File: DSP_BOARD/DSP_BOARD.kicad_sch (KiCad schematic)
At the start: 0 parts

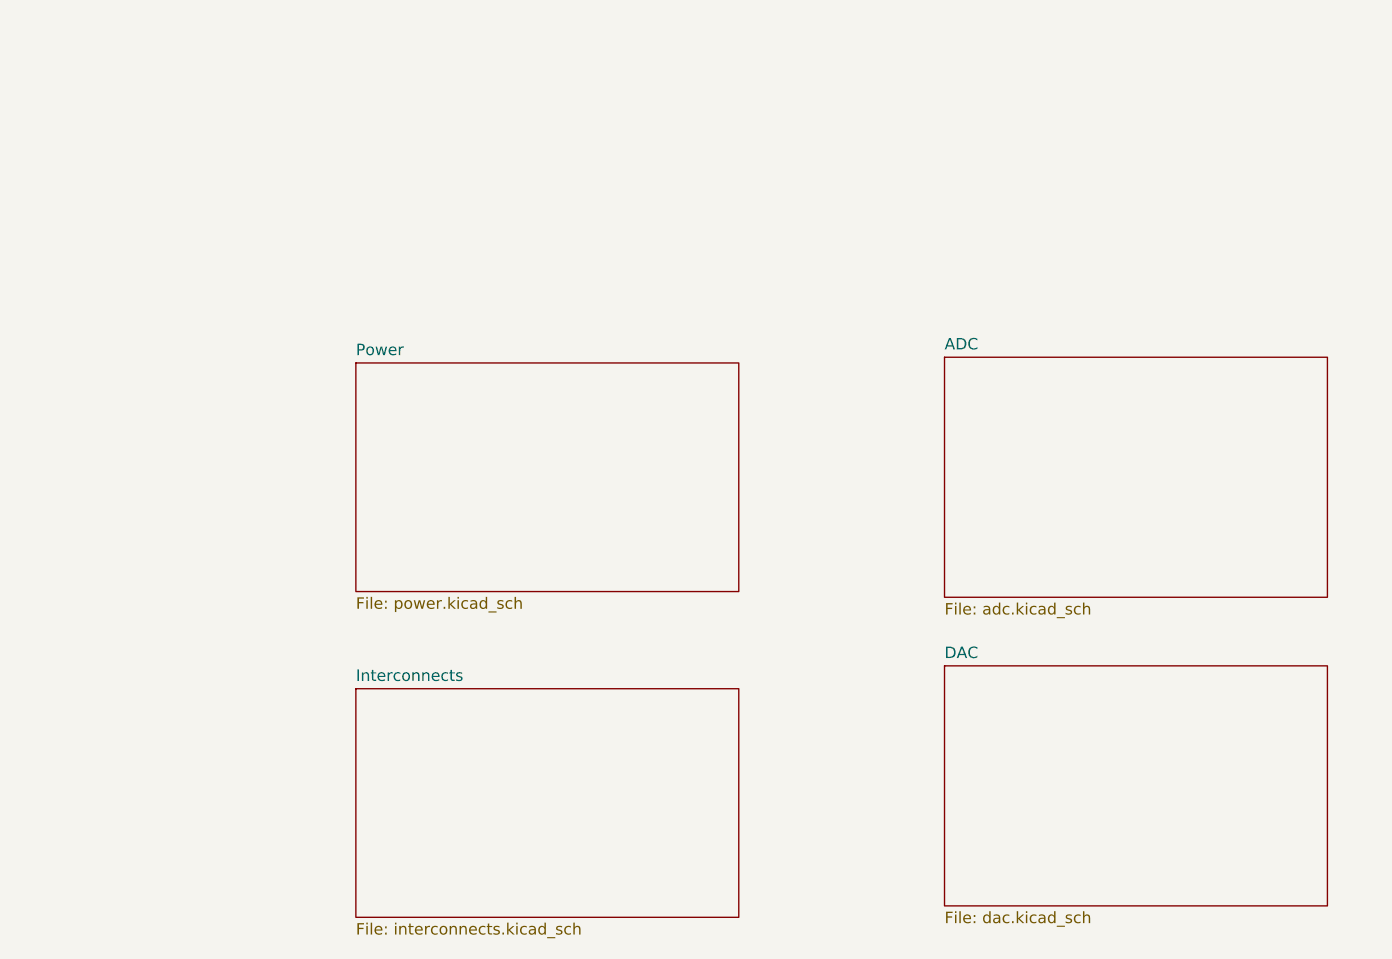
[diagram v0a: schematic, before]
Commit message: somewhat started on the DSP board, added in ADC, DAC and Tz170 symbols and footprints
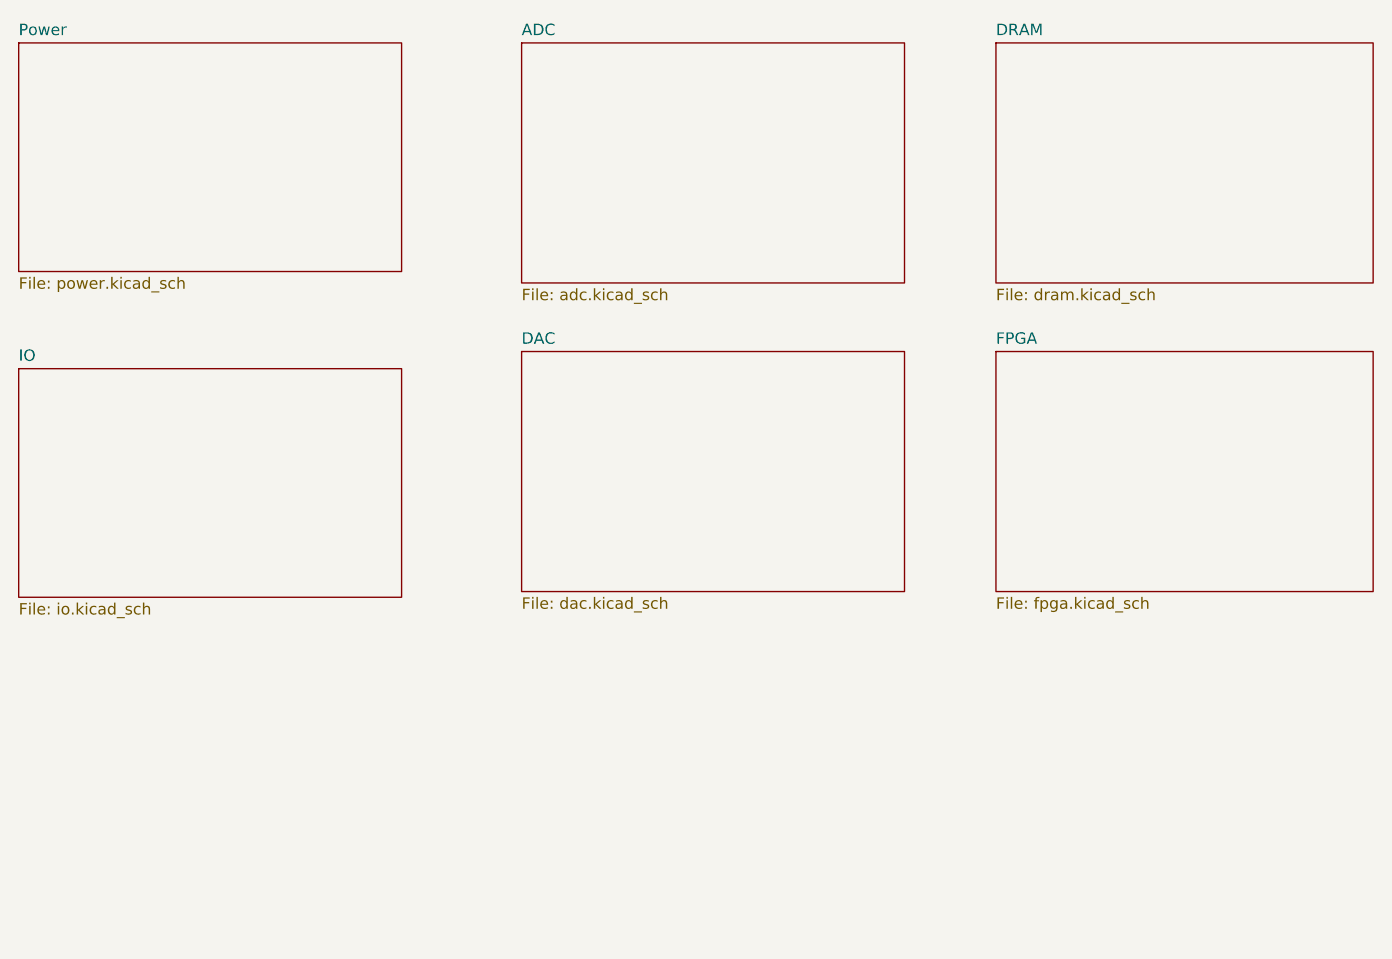
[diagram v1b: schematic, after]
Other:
- sheet Interconnects renamed IO
- added sheet DRAM (dram.kicad_sch)
- added sheet FPGA (fpga.kicad_sch)
- sheet IO: file interconnects.kicad_sch -> io.kicad_sch
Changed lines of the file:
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@@
 	(paper "A4")
 	(sheet
-		(at 134.62 102.235)
+		(at 140.335 67.31)
+		(size 41.91 26.67)
+		(exclude_from_sim no)
+		(in_bom yes)
+		(on_board yes)
+		(dnp no)
+		(fields_autoplaced yes)
+		(stroke
+			(width 0.1524)
+			(type solid)
+		)
+		(fill
+			(color 0 0 0 0)
+		)
+		(property "Sheetname" "FPGA"
+			(at 140.335 66.5984 0)
+			(show_name no)
+			(do_not_autoplace no)
+			(effects
+				(font
+					(size 1.27 1.27)
+				)
+				(justify left bottom)
+			)
+		)
+		(property "Sheetfile" "fpga.kicad_sch"
+			(at 140.335 94.5646 0)
+			(show_name no)
+			(do_not_autoplace no)
+			(effects
+				(font
+					(size 1.27 1.27)
+				)
+				(justify left top)
+			)
+		)
+		(instances
+			(project "DSP_BOARD"
+				(path "/d0a47c1b-0993-4eef-849f-6ae6ee99c242"
+					(page "7")
+				)
+			)
+		)
+	)
+	(sheet
+		(at 87.63 67.31)
 		(size 42.545 26.67)
 		(exclude_from_sim no)
@@
 		)
 		(property "Sheetname" "DAC"
-			(at 134.62 101.5234 0)
+			(at 87.63 66.5984 0)
 			(show_name no)
 			(do_not_autoplace no)
@@
 		)
 		(property "Sheetfile" "dac.kicad_sch"
-			(at 134.62 129.4896 0)
+			(at 87.63 94.5646 0)
 			(show_name no)
 			(do_not_autoplace no)
@@
 	)
 	(sheet
-		(at 69.215 104.775)
+		(at 31.75 69.215)
 		(size 42.545 25.4)
 		(exclude_from_sim no)
@@
 			(color 0 0 0 0)
 		)
-		(property "Sheetname" "Interconnects"
-			(at 69.215 104.0634 0)
-			(show_name no)
-			(do_not_autoplace no)
-			(effects
-				(font
-					(size 1.27 1.27)
-				)
-				(justify left bottom)
-			)
-		)
-		(property "Sheetfile" "interconnects.kicad_sch"
-			(at 69.215 130.7596 0)
+		(property "Sheetname" "IO"
+			(at 31.75 68.5034 0)
+			(show_name no)
+			(do_not_autoplace no)
+			(effects
+				(font
+					(size 1.27 1.27)
+				)
+				(justify left bottom)
+			)
+		)
+		(property "Sheetfile" "io.kicad_sch"
+			(at 31.75 95.1996 0)
 			(show_name no)
 			(do_not_autoplace no)
@@
 	)
 	(sheet
-		(at 69.215 68.58)
+		(at 140.335 33.02)
+		(size 41.91 26.67)
+		(exclude_from_sim no)
+		(in_bom yes)
+		(on_board yes)
+		(dnp no)
+		(fields_autoplaced yes)
+		(stroke
+			(width 0.1524)
+			(type solid)
+		)
+		(fill
+			(color 0 0 0 0)
+		)
+		(property "Sheetname" "DRAM"
+			(at 140.335 32.3084 0)
+			(show_name no)
+			(do_not_autoplace no)
+			(effects
+				(font
+					(size 1.27 1.27)
+				)
+				(justify left bottom)
+			)
+		)
+		(property "Sheetfile" "dram.kicad_sch"
+			(at 140.335 60.2746 0)
+			(show_name no)
+			(do_not_autoplace no)
+			(effects
+				(font
+					(size 1.27 1.27)
+				)
+				(justify left top)
+			)
+		)
+		(instances
+			(project "DSP_BOARD"
+				(path "/d0a47c1b-0993-4eef-849f-6ae6ee99c242"
+					(page "6")
+				)
+			)
+		)
+	)
+	(sheet
+		(at 31.75 33.02)
 		(size 42.545 25.4)
 		(exclude_from_sim no)
@@
 		)
 		(property "Sheetname" "Power"
-			(at 69.215 67.8684 0)
+			(at 31.75 32.3084 0)
 			(show_name no)
 			(do_not_autoplace no)
@@
 		)
 		(property "Sheetfile" "power.kicad_sch"
-			(at 69.215 94.5646 0)
+			(at 31.75 59.0046 0)
 			(show_name no)
 			(do_not_autoplace no)
@@
 	)
 	(sheet
-		(at 134.62 67.945)
+		(at 87.63 33.02)
 		(size 42.545 26.67)
 		(exclude_from_sim no)
@@
 		)
 		(property "Sheetname" "ADC"
-			(at 134.62 67.2334 0)
+			(at 87.63 32.3084 0)
 			(show_name no)
 			(do_not_autoplace no)
@@
 		)
 		(property "Sheetfile" "adc.kicad_sch"
-			(at 134.62 95.1996 0)
-			(show_name no)
-			(do_not_autoplace no)
+			(at 87.63 60.2746 0)
+			(show_name no)
+			(do_not_autoplace no)
